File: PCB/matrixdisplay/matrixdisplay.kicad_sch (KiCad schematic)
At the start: 94 parts, among them J1 FILAS, J2 COLUMNAS, J3 SWD, J4 USART, J5 FILAS, J6 COL, SW1 BOOT0, SW2 P_ON, SW3 BT1, SW4 BT2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

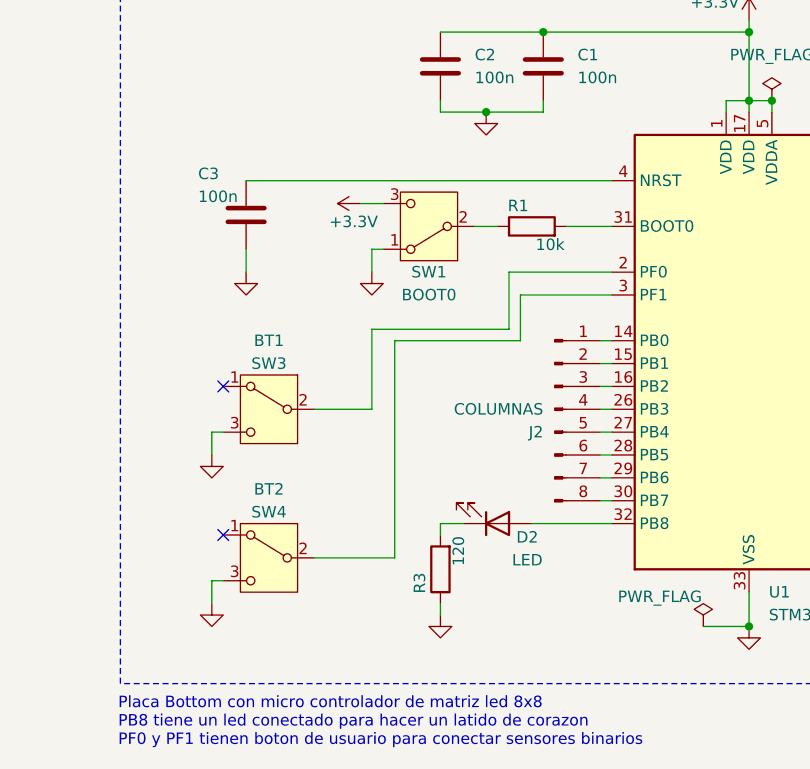
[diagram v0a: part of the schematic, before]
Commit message: Modify buttons and mounting holes
BOOT0 was removed in favor of default boot mode
User Buttons replaced to horizontal aligment for easier access

Mounting Holes changed to M2 instead of M3 standard
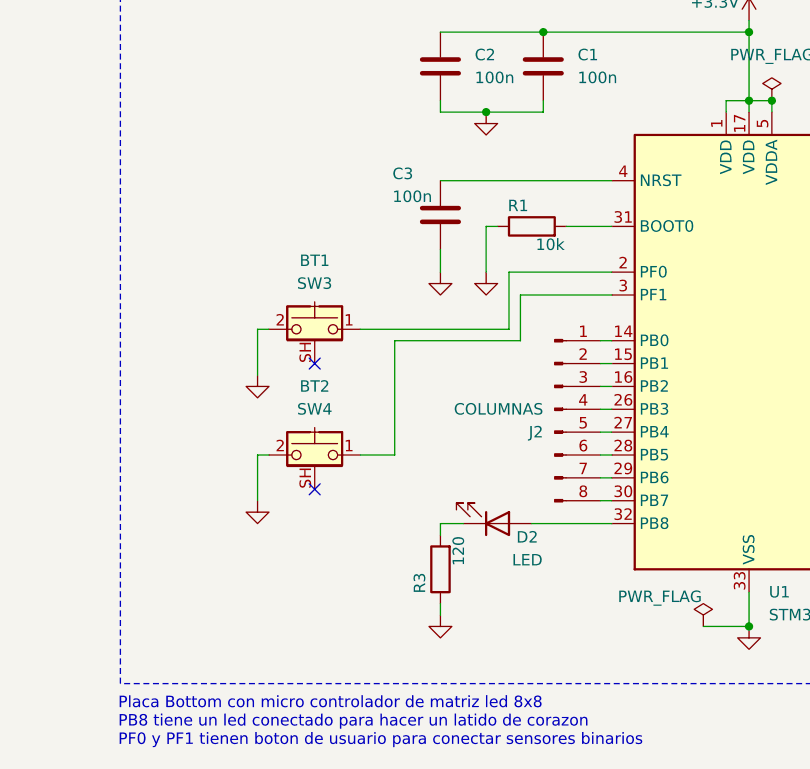
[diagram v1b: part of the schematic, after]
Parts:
- removed SW1: BOOT0, Button_Switch_SMD:SW_SPST_B3U-1100P, symbol Switch:SW_SPDT
- H1, H2: footprint MountingHole:MountingHole_3.2mm_M3 -> MountingHole:MountingHole_2mm
- SW3, SW4: footprint Button_Switch_SMD:SW_SPST_B3U-1100P -> SamacSys_Parts:TS24CA; symbol Switch:SW_SPDT -> Switch:SW_Push_Shielded
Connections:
- net GND: now also R1.1, SW3.2, SW4.2; no longer SW3.3 (C), SW4.3 (C)
- net at SW4.1: now also U1.3 (PF1)
- net at U1.2 (PF0): now also SW3.1; no longer SW3.2 (B)
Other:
- moved on the sheet: C3
